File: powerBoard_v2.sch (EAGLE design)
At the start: 25 parts, among them U1 TLE2426CD

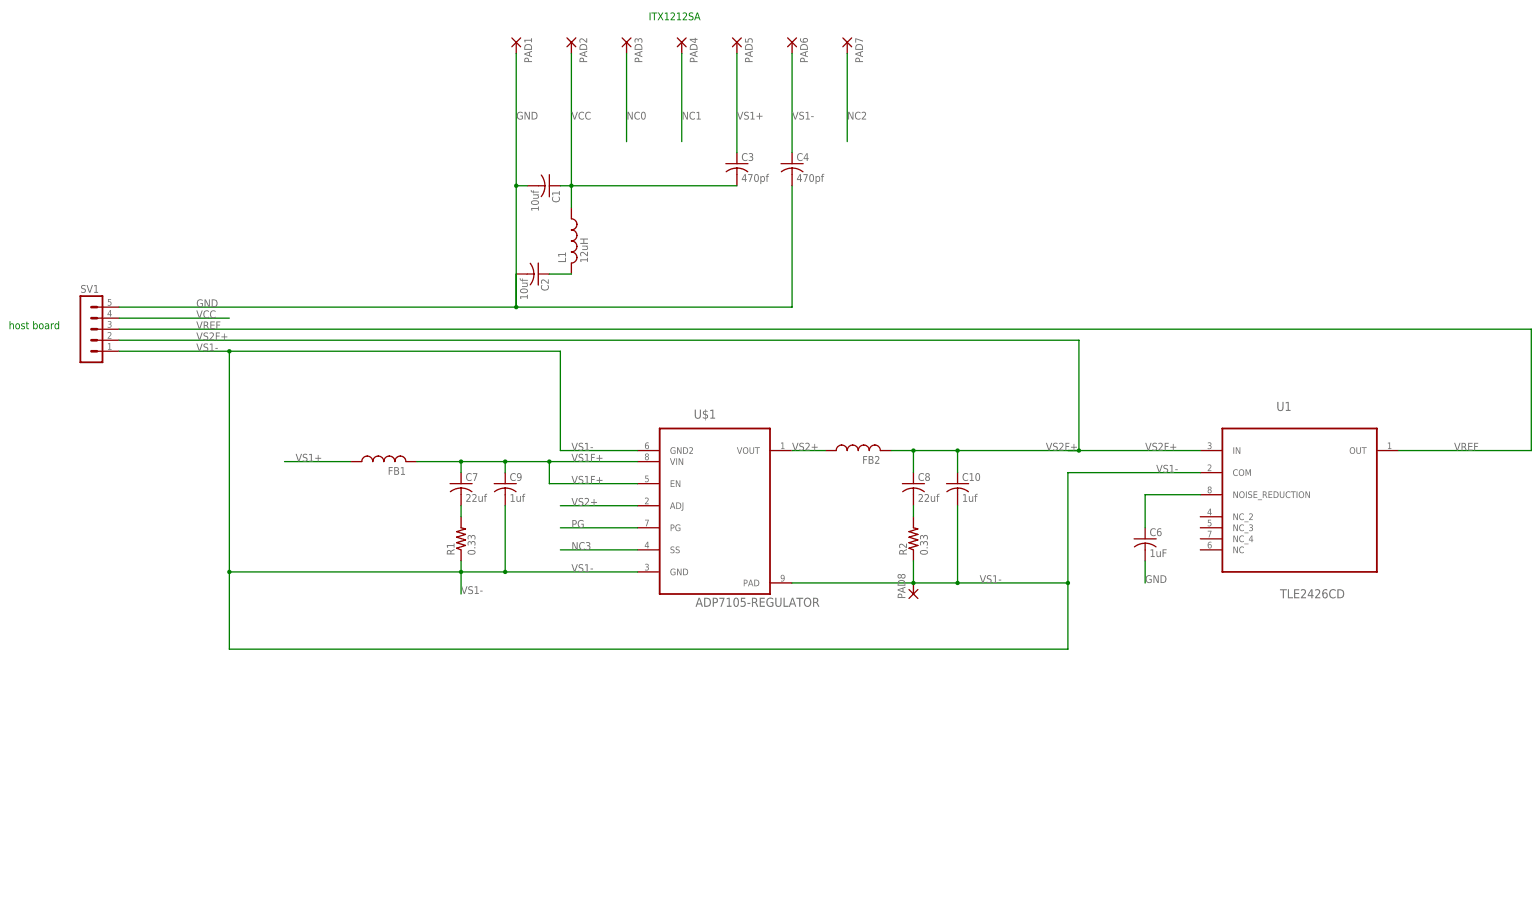
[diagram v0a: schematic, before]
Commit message: updated power board designs: v2 uses low current 2.5v reference, v3 uses 10v rail and 5v ref both with simple linear regulators. Added breakout board to go from DB37 to BNC
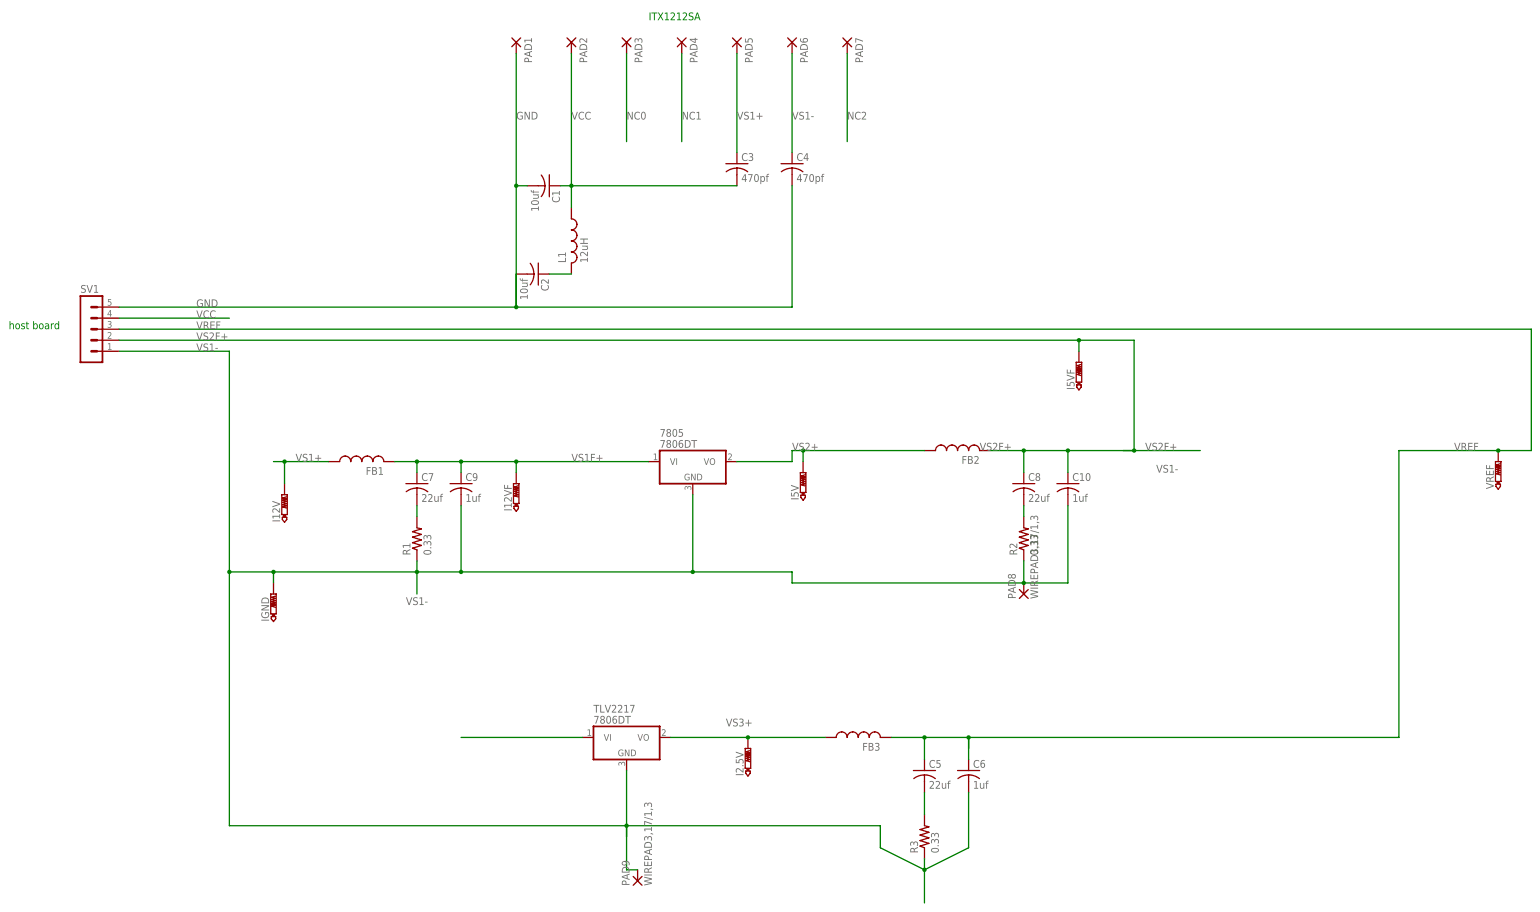
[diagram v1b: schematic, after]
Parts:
- removed U$1: ADP7105-REGULATOR, tuckerLib:ADP7105-REGULATOR
- removed U1: TLE2426CD, Texas Instruments_By_element14_Batch_1:TLE2426CD
- added 7805, TLV2217: 7806DT, linear:7806DT
- added C5: 22uf, rcl:C-USC0805K
- added FB3: (no value), rcl:L-USL2012C
- added I12V, I12VF, I2.5V, I5V, I5VF, IGND, VREF: PTR1PAD1-13, testpad:PTR1PAD1-13
- added PAD9: WIREPAD3,17/1,3, wirepad:WIREPAD3,17/1,3
- added R3: 0.33, resistor:R-US_R2012W
- C6: value 1uF -> 1uf; device rcl:C-USC0805 -> rcl:C-USC0805K
- PAD8: value (none) -> WIREPAD3,17/1,3; device wirepad:2,54/1,1 -> wirepad:WIREPAD3,17/1,3
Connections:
- removed net NC3: U$1.SS
- removed net PG: U$1.PG
- new net VS3+: FB3.1, I2.5V.TP, TLV2217.VO
- net GND: no longer C6.2
- net N$2: now also C5.2, R3.2; no longer C6.1, U1.NOISE_REDUCTION
- net VREF: now also C5.1, C6.1, FB3.2, VREF.TP; no longer U1.OUT
- net VS1+: now also I12V.TP
- net VS1-: now also 7805.GND, C6.2, IGND.TP, PAD9.P, R3.1, TLV2217.GND; no longer U$1.GND, U$1.GND2, U$1.PAD, U1.COM
- net VS1F+: now also 7805.VI, I12VF.TP, TLV2217.VI; no longer U$1.EN, U$1.VIN
- net VS2+: now also 7805.VO, I5V.TP; no longer U$1.ADJ, U$1.VOUT
- net VS2F+: now also I5VF.TP; no longer U1.IN
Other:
- moved on the sheet: C10, C6, C7, C8, C9, FB1, FB2, R1, R2
